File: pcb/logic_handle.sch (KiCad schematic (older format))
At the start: 13 parts, among them U1 NCP1117-3.3_TO252

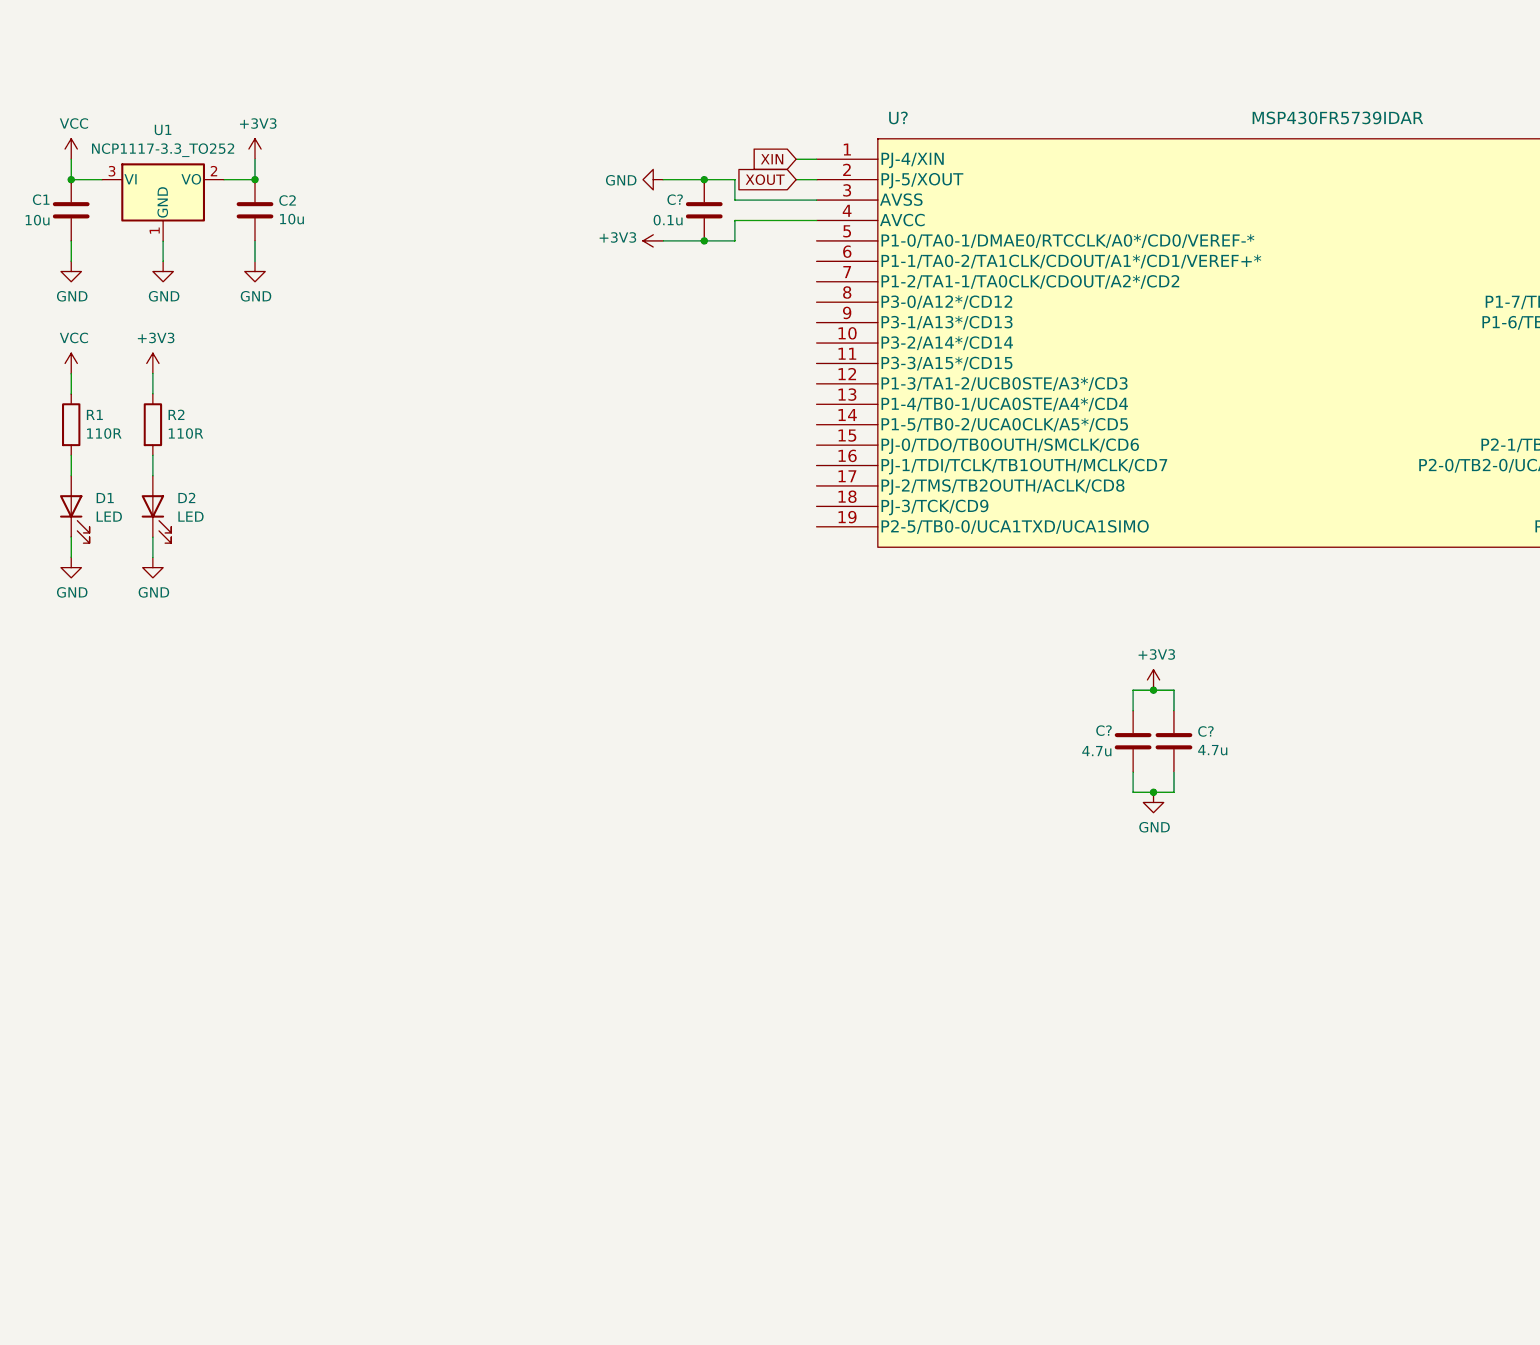
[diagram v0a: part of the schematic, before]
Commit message: [WIP] logic handle voltage translator
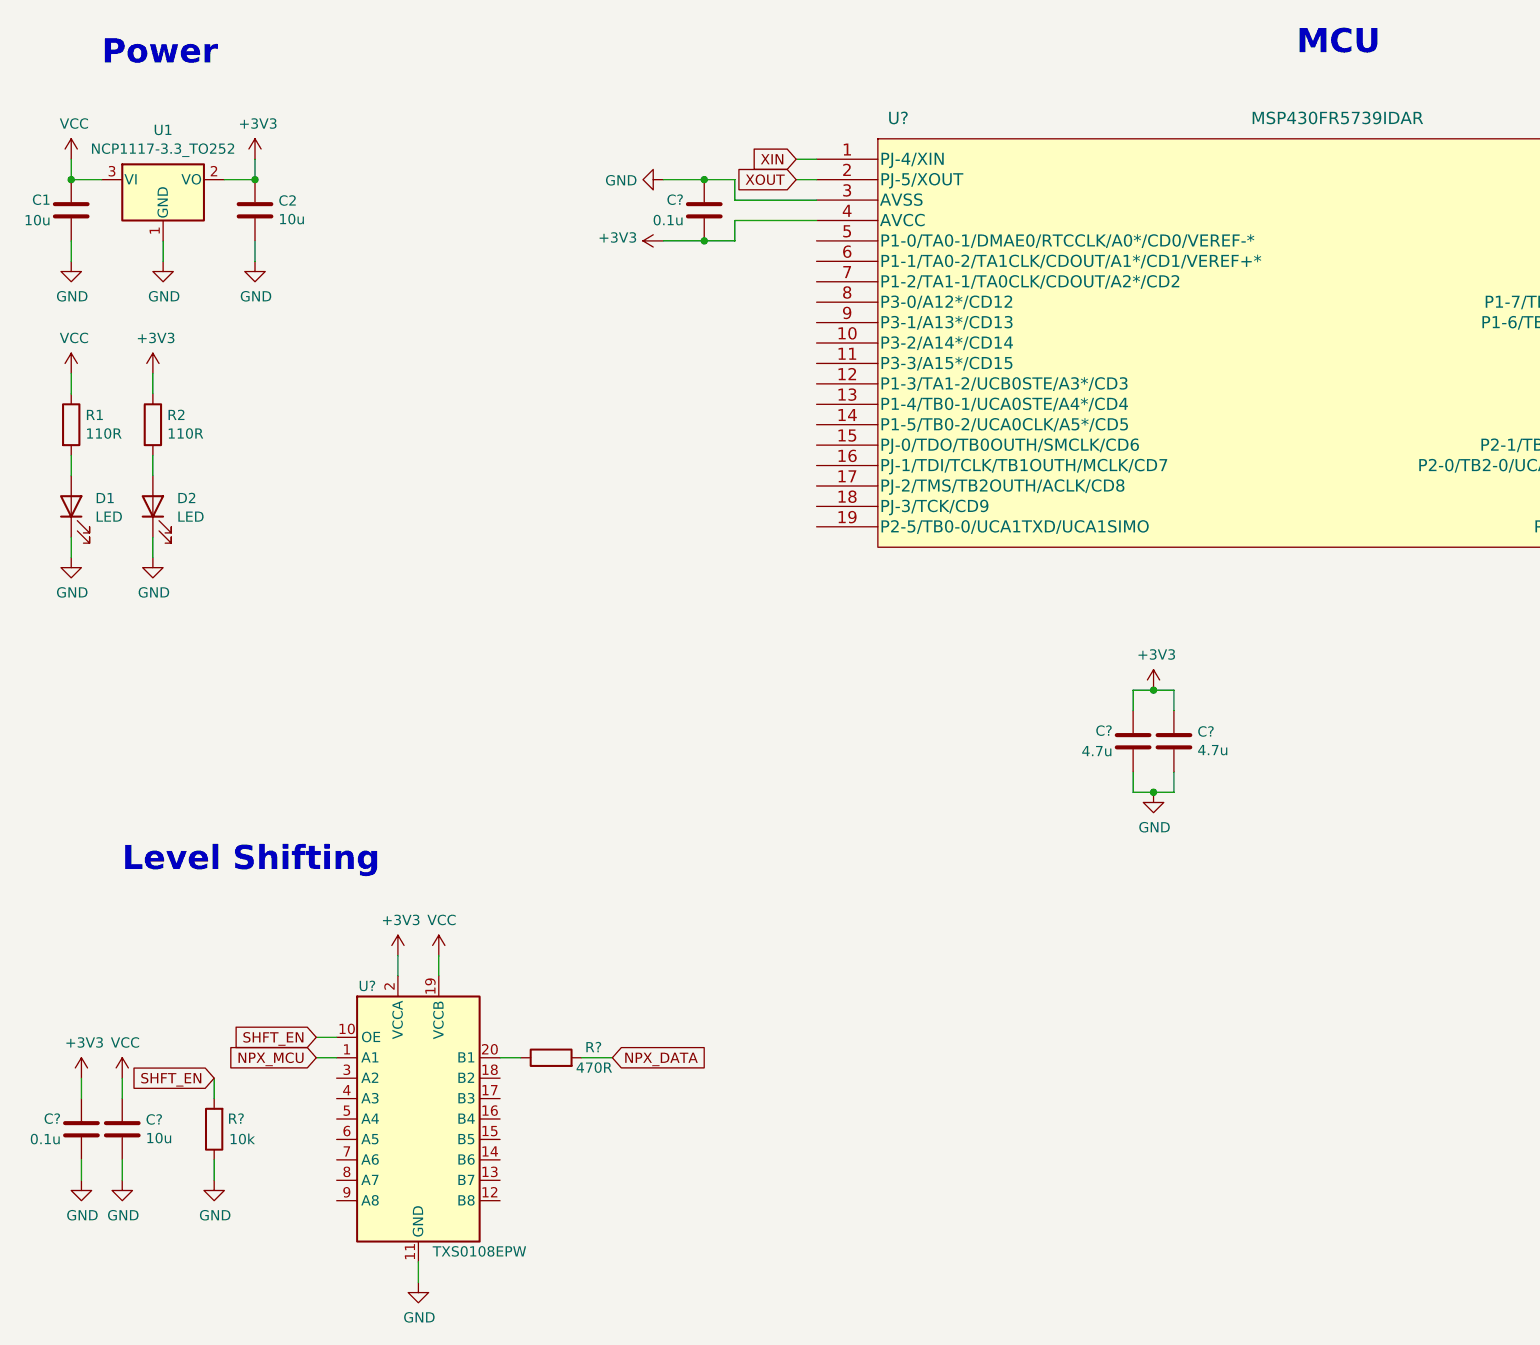
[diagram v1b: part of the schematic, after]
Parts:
- added C?: 0.1u, symbol Device:C
- added C?: 10u, symbol Device:C
- added R?: 10k, symbol Device:R
- added R?: 470R, symbol Device:R
- added U?: TXS0108EPW, Package_SO:TSSOP-20_4.4x6.5mm_P0.65mm, symbol Logic_LevelTranslator:TXS0108EPW
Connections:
- net +3V3: now also C?.2, U?.2 (VCCA)
- net GND: now also C?.1, C?.2, R?.1, U?.11 (GND)
- net VCC: now also C?.1, U?.19 (VCCB)
- new net: R?.1, U?.20 (B1)
- new net NPX_DATA: R?.2
- new net NPX_MCU: U?.1 (A1)
- new net SHFT_EN: R?.2, U?.10 (OE)
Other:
- note added: "Level Shifting"
- note added: "MCU"
- note added: "Power"
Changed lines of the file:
@@
 	6550 4450 6550 4350
 Connection ~ 6450 4450
+$Comp
+L Logic_LevelTranslator:TXS0108EPW U?
+U 1 1 619CE39A
+P 2850 6050
+F 0 "U?" H 2600 6700 50  0000 C CNN
+F 1 "TXS0108EPW" H 3150 5400 50  0000 C CNN
+F 2 "Package_SO:TSSOP-20_4.4x6.5mm_P0.65mm" H 2850 5300 50  0001 C CNN
+F 3 "www.ti.com/lit/ds/symlink/txs0108e.pdf" H 2850 5950 50  0001 C CNN
+F 4 "296-21527-1-ND" H 2850 6050 50  0001 C CNN "Digikey"
+	1    2850 6050
+	1    0    0    -1
+$EndComp
+$Comp
+L power:+3V3 #PWR?
+U 1 1 619CF59A
+P 2750 5250
+F 0 "#PWR?" H 2750 5100 50  0001 C CNN
+F 1 "+3V3" H 2765 5423 50  0000 C CNN
+F 2 "" H 2750 5250 50  0001 C CNN
+F 3 "" H 2750 5250 50  0001 C CNN
+	1    2750 5250
+	1    0    0    -1
+$EndComp
+Wire Wire Line
+	2750 5350 2750 5250
+$Comp
+L power:VCC #PWR?
+U 1 1 619D199B
+P 2950 5250
+F 0 "#PWR?" H 2950 5100 50  0001 C CNN
+F 1 "VCC" H 2965 5423 50  0000 C CNN
+F 2 "" H 2950 5250 50  0001 C CNN
+F 3 "" H 2950 5250 50  0001 C CNN
+	1    2950 5250
+	1    0    0    -1
+$EndComp
+Wire Wire Line
+	2950 5350 2950 5250
+$Comp
+L Device:R R?
+U 1 1 619D30A3
+P 1850 6100
+F 0 "R?" H 1700 6050 50  0000 L CNN
+F 1 "10k" H 1650 6150 50  0000 L CNN
+F 2 "" V 1780 6100 50  0001 C CNN
+F 3 "https://www.seielect.com/catalog/sei-rmcf_rmcp.pdf" H 1850 6100 50  0001 C CNN
+F 4 "RMCF0805JT110RCT-ND" H 1850 6100 50  0001 C CNN "Digikey"
+	1    1850 6100
+	-1   0    0    1
+$EndComp
+$Comp
+L power:GND #PWR?
+U 1 1 619D40ED
+P 1850 6350
+F 0 "#PWR?" H 1850 6100 50  0001 C CNN
+F 1 "GND" H 1855 6177 50  0000 C CNN
+F 2 "" H 1850 6350 50  0001 C CNN
+F 3 "" H 1850 6350 50  0001 C CNN
+	1    1850 6350
+	1    0    0    -1
+$EndComp
+Text GLabel 2350 5650 0    50   Input ~ 0
+SHFT_EN
+$Comp
+L power:GND #PWR?
+U 1 1 619D79C2
+P 2850 6850
+F 0 "#PWR?" H 2850 6600 50  0001 C CNN
+F 1 "GND" H 2855 6677 50  0000 C CNN
+F 2 "" H 2850 6850 50  0001 C CNN
+F 3 "" H 2850 6850 50  0001 C CNN
+	1    2850 6850
+	1    0    0    -1
+$EndComp
+Wire Wire Line
+	2850 6750 2850 6850
+$Comp
+L Device:C C?
+U 1 1 619D9BB2
+P 1200 6100
+F 0 "C?" H 1300 6050 50  0000 L CNN
+F 1 "0.1u" H 1300 6150 50  0000 L CNN
+F 2 "" H 1238 5950 50  0001 C CNN
+F 3 "~" H 1200 6100 50  0001 C CNN
+	1    1200 6100
+	-1   0    0    1
+$EndComp
+$Comp
+L power:GND #PWR?
+U 1 1 619DC720
+P 1200 6350
+F 0 "#PWR?" H 1200 6100 50  0001 C CNN
+F 1 "GND" H 1205 6177 50  0000 C CNN
+F 2 "" H 1200 6350 50  0001 C CNN
+F 3 "" H 1200 6350 50  0001 C CNN
+	1    1200 6350
+	1    0    0    -1
+$EndComp
+$Comp
+L power:GND #PWR?
+U 1 1 619DD6CD
+P 1400 6350
+F 0 "#PWR?" H 1400 6100 50  0001 C CNN
+F 1 "GND" H 1405 6177 50  0000 C CNN
+F 2 "" H 1400 6350 50  0001 C CNN
+F 3 "" H 1400 6350 50  0001 C CNN
+	1    1400 6350
+	1    0    0    -1
+$EndComp
+Wire Wire Line
+	1200 6350 1200 6250
+Wire Wire Line
+	1400 6350 1400 6250
+$Comp
+L Device:C C?
+U 1 1 619DFAAB
+P 1400 6100
+F 0 "C?" H 1515 6146 50  0000 L CNN
+F 1 "10u" H 1515 6055 50  0000 L CNN
+F 2 "" H 1438 5950 50  0001 C CNN
+F 3 "~" H 1400 6100 50  0001 C CNN
+	1    1400 6100
+	1    0    0    -1
+$EndComp
+$Comp
+L power:+3V3 #PWR?
+U 1 1 619E1DEA
+P 1200 5850
+F 0 "#PWR?" H 1200 5700 50  0001 C CNN
+F 1 "+3V3" H 1215 6023 50  0000 C CNN
+F 2 "" H 1200 5850 50  0001 C CNN
+F 3 "" H 1200 5850 50  0001 C CNN
+	1    1200 5850
+	1    0    0    -1
+$EndComp
+$Comp
+L power:VCC #PWR?
+U 1 1 619E251A
+P 1400 5850
+F 0 "#PWR?" H 1400 5700 50  0001 C CNN
+F 1 "VCC" H 1415 6023 50  0000 C CNN
+F 2 "" H 1400 5850 50  0001 C CNN
+F 3 "" H 1400 5850 50  0001 C CNN
+	1    1400 5850
+	1    0    0    -1
+$EndComp
+Wire Wire Line
+	1200 5850 1200 5950
+Wire Wire Line
+	1400 5850 1400 5950
+Text Notes 1400 4850 0    118  ~ 24
+Level Shifting
+Text Notes 7150 850  0    118  ~ 24
+MCU
+Text Notes 1300 900  0    118  ~ 24
+Power
+$Comp
+L Device:R R?
+U 1 1 619F32E8
+P 3500 5750
+F 0 "R?" V 3550 5500 50  0000 L CNN
+F 1 "470R" V 3450 5450 50  0000 L CNN
+F 2 "" V 3430 5750 50  0001 C CNN
+F 3 "https://www.seielect.com/catalog/sei-rmcf_rmcp.pdf" H 3500 5750 50  0001 C CNN
+F 4 "RMCF0805JT110RCT-ND" H 3500 5750 50  0001 C CNN "Digikey"
+	1    3500 5750
+	0    -1   -1   0
+$EndComp
+Wire Wire Line
+	3350 5750 3250 5750
+Wire Wire Line
+	3650 5750 3800 5750
+Text GLabel 3800 5750 2    50   Input ~ 0
+NPX_DATA
+Text GLabel 2350 5750 0    50   Input ~ 0
+NPX_MCU
+Wire Wire Line
+	1850 6250 1850 6350
+Text GLabel 1850 5850 0    50   Input ~ 0
+SHFT_EN
+Wire Wire Line
+	1850 5850 1850 5950
+Wire Wire Line
+	2350 5650 2450 5650
+Wire Wire Line
+	2350 5750 2450 5750
 $EndSCHEMATC

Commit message: [WIP]: Logic handle schematic and layout complete
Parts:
- added C8, C9: 15p, Capacitor_SMD:C_0805_2012Metric, symbol Device:C
- added J1: Conn_01x05_Male, Connector_PinHeader_2.54mm:PinHeader_1x05_P2.54mm_Vertical, symbol Connector:Conn_01x05_Male
- added JP1, JP10, JP2, JP3, JP4, JP5, JP6, JP7, JP8, JP9: Jumper_3_Bridged12, Jumper:SolderJumper-3_P1.3mm_Bridged2Bar12_Pad1.0x1.5mm, symbol Jumper:Jumper_3_Bridged12
- added JP11: Jumper, Jumper:SolderJumper-2_P1.3mm_Bridged2Bar_Pad1.0x1.5mm, symbol Device:Jumper
- added Q1: BSS214NW, Package_TO_SOT_SMD:SOT-323_SC-70, symbol Transistor_FET:BSS214NW
- added R5: 47k, Resistor_SMD:R_0805_2012Metric, symbol Device:R
- added R6, R8: 10k, Resistor_SMD:R_0805_2012Metric, symbol Device:R
- added R7: 110R, Resistor_SMD:R_0805_2012Metric, symbol Device:R
- added R9: 1M, Resistor_SMD:R_0805_2012Metric, symbol Device:R
- added SW1: SW_Push, Button_Switch_SMD:SW_SPST_TL3342, symbol Switch:SW_Push
- added TP1, TP10, TP11, TP12, TP2, TP3, TP4, TP5, TP6, TP7, TP8, TP9: TestPoint, TestPoint:TestPoint_Pad_2.0x2.0mm, symbol Connector:TestPoint
- added Y1: Crystal, Gigahawk:Crystal_SMD_AWSZT-CV-2Pin_3.7x3.1mm, symbol Device:Crystal
- C1, C2: footprint (none) -> Capacitor_SMD:C_0805_2012Metric
- C10, C11, C3, C4, C5, C6, C7: renamed from C?; footprint (none) -> Capacitor_SMD:C_0805_2012Metric
- R1, R2: footprint (none) -> Resistor_SMD:R_0805_2012Metric
- R3, R4: renamed from R?; footprint (none) -> Resistor_SMD:R_0805_2012Metric
- gave numbers to parts that had none: 2
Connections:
- net +3V3: now also R5.2, TP2.1
- net GND: now also C8.2, C9.1, J1.4 (Pin_4), JP11.1, Q1.3 (D), R8.1, SW1.2, TP3.1
- net NPX_MCU: now also JP1.2 (C), JP6.2 (C); no longer U2.1 (A1)
- net SBWTCK: now also J1.2 (Pin_2)
- net SBWTDIO: now also J1.3 (Pin_3), R5.1, SW1.1
- net SHFT_EN: now also U3.29 (P3-7/TB2-2), TP11.1
- net VCC: now also R6.2, R7.2, TP1.1
- net XIN: now also C8.1, R9.1, Y1.1
- net XOUT: now also C9.2, R9.2, Y1.2
- net BTN1_AUX: now reaches U3.10 (P3-2/A14*/CD14)
- net BTN1_AUX: now also JP4.3 (B)
- net BTN2_AUX: now reaches U3.11 (P3-3/A15*/CD15)
- net BTN2_AUX: now also JP5.3 (B)
- net NPX_DBG_CLK_AUX: now reaches U3.14 (P1-5/TB0-2/UCA0CLK/A5*/CD5)
- net NPX_DBG_CLK_AUX: now also TP5.1
- net LED1_MAIN: now reaches U3.15 (PJ-0/TDO/TB0OUTH/SMCLK/CD6)
- net LED1_MAIN: now also JP2.1 (A)
- net LED2_MAIN: now reaches U3.16 (PJ-1/TDI/TCLK/TB1OUTH/MCLK/CD7)
- net LED2_MAIN: now also JP3.1 (A)
- net LED1_AUX: now reaches U3.17 (PJ-2/TMS/TB2OUTH/ACLK/CD8)
- net LED1_AUX: now also JP2.3 (B)
- net LED2_AUX: now reaches U3.18 (PJ-3/TCK/CD9)
- net LED2_AUX: now also JP3.3 (B)
- net UART_TXD: now reaches U3.19 (P2-5/TB0-0/UCA1TXD/UCA1SIMO)
- net UART_TXD: now also J1.1 (Pin_1)
- net UART_RXD: now reaches U3.20 (P2-6/TB1-0/UCA1RXD/UCA1SOMI)
- net UART_RXD: now also J1.5 (Pin_5)
- net NPX_AUX: now reaches U3.23 (P2-0/TB2-0/UCA0TXD/UCA0SIMO/TB0CLK/ACLK)
- net NPX_AUX: now also JP1.3 (B)
- net NPX_DBG_CLK_MAIN: now reaches U3.25 (P2-2/TB2-2/UCB0CLK/TB1-0)
- net NPX_DBG_CLK_MAIN: now also TP4.1
- net NPX_MAIN: now reaches U3.30 (P1-6/TB1-1/UCB0SIMO/UCB0SDA/TA0-0)
- net NPX_MAIN: now also JP1.1 (A)
- net BTN1_MAIN: now reaches U3.8 (P3-0/A12*/CD12)
- net BTN1_MAIN: now also JP4.1 (A)
- net BTN2_MAIN: now reaches U3.9 (P3-1/A13*/CD13)
- net BTN2_MAIN: now also JP5.1 (A)
- net BTN2: now reaches U2.15 (B5)
- net BTN2: now also JP10.3 (B), TP10.1
- net BTN+: now reaches U2.16 (B4)
- net BTN+: now also JP9.3 (B), R6.1, TP9.1
- net IC_BTN_LED: now reaches U2.17 (B3)
- net IC_BTN_LED: now also JP8.3 (B), TP8.1
- net LED1: now reaches U2.18 (B2)
- net LED1: now also JP7.3 (B), Q1.1 (G), R8.2, TP7.1
- net NPX_MCU_BYPASS: now reaches R4.1, U2.20 (B1)
- net NPX_MCU_BYPASS: now also JP6.3 (B), TP12.1
- net LED1_MCU_SHIFT: now reaches U2.3 (A2)
- net LED1_MCU_SHIFT: now also JP7.1 (A)
- net LED2_MCU_SHIFT: now reaches U2.4 (A3)
- net LED2_MCU_SHIFT: now also JP8.1 (A)
- net BTN1_MCU_SHIFT: now reaches U2.5 (A4)
- net BTN1_MCU_SHIFT: now also JP9.1 (A)
- net BTN2_MCU_SHIFT: now reaches U2.6 (A5)
- net BTN2_MCU_SHIFT: now also JP10.1 (A)
- net NPX_DATA renamed NPX
- net NPX: now also TP6.1
- new net BTN-: JP11.2
- new net BTN1_MCU: JP4.2 (C), JP9.2 (C)
- new net BTN2_MCU: JP10.2 (C), JP5.2 (C)
- new net LED+: R7.1
- new net LED-: Q1.2 (S)
- new net LED1_MCU: JP2.2 (C), JP7.2 (C)
- new net LED2_MCU: JP3.2 (C), JP8.2 (C)
- new net NPX_MCU_SHIFT: JP6.1 (A), U2.1 (A1)
- no-connect marks 0 -> 19
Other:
- note added: "24MHz or DNI"
- note added: "Jumper here to avoid\nGND net being renamed"
- note added: "Level Shifter Bypass"
- note added: "Programming"
- note added: "Reset\nSwitch"
- moved on the sheet: C3, C4, C6, C7, R3, R4, U2

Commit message: [WIP]: Finish logic PCB
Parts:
- C1, C2, C4: Digikey (none) -> 1276-6456-1-ND
- C10: Digikey (none) -> 478-10438-1-ND
- C11, C3, C5: Digikey (none) -> 478-10836-1-ND
- C6, C7: Digikey (none) -> 1276-1259-1-ND
- C8, C9: Digikey (none) -> 478-1306-1-ND
- U3: Digikey (none) -> 296-29235-1-ND
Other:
- note added: "Common"
- note added: "Testpoints"
- moved on the sheet: TP1, TP10, TP11, TP12, TP2, TP3, TP4, TP5, TP6, TP7, TP8, TP9

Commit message: pcb: Cleanup BOM items (#7)
Replaced out of stock components with substitutes
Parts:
- R3, R6, R8: Digikey RMCF0805JT110RCT-ND -> RMCF0805JT10K0CT-ND
- R4: Digikey RMCF0805JT110RCT-ND -> A129745CT-ND
- R5: Digikey RMCF0805JT110RCT-ND -> A130144CT-ND
- R9: Digikey RMCF0805JT110RCT-ND -> A106058CT-ND
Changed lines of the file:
@@
 F 2 "Resistor_SMD:R_0805_2012Metric" V 1380 4500 50  0001 C CNN
 F 3 "https://www.seielect.com/catalog/sei-rmcf_rmcp.pdf" H 1450 4500 50  0001 C CNN
-F 4 "RMCF0805JT110RCT-ND" H 1450 4500 50  0001 C CNN "Digikey"
+F 4 "RMCF0805JT10K0CT-ND" H 1450 4500 50  0001 C CNN "Digikey"
 	1    1450 4500
 	-1   0    0    1
@@
 F 1 "470R" V 3450 4500 50  0000 L CNN
 F 2 "Resistor_SMD:R_0805_2012Metric" V 3430 4800 50  0001 C CNN
-F 3 "https://www.seielect.com/catalog/sei-rmcf_rmcp.pdf" H 3500 4800 50  0001 C CNN
-F 4 "RMCF0805JT110RCT-ND" H 3500 4800 50  0001 C CNN "Digikey"
+F 3 "https://www.te.com/commerce/DocumentDelivery/DDEController?Action=srchrtrv&DocNm=1773204-3&DocType=DS&DocLang=English" H 3500 4800 50  0001 C CNN
+F 4 "A129745CT-ND" H 3500 4800 50  0001 C CNN "Digikey"
 	1    3500 4800
 	0    -1   -1   0
@@
 F 1 "1M" V 9650 4100 50  0000 L CNN
 F 2 "Resistor_SMD:R_0805_2012Metric" V 9530 4000 50  0001 C CNN
-F 3 "https://www.seielect.com/catalog/sei-rmcf_rmcp.pdf" H 9600 4000 50  0001 C CNN
-F 4 "RMCF0805JT110RCT-ND" H 9600 4000 50  0001 C CNN "Digikey"
+F 3 "https://www.te.com/commerce/DocumentDelivery/DDEController?Action=srchrtrv&DocNm=1773204&DocType=DS&DocLang=English" H 9600 4000 50  0001 C CNN
+F 4 "A106058CT-ND" H 9600 4000 50  0001 C CNN "Digikey"
 	1    9600 4000
 	0    -1   -1   0
@@
 F 2 "Resistor_SMD:R_0805_2012Metric" V 8030 7850 50  0001 C CNN
 F 3 "https://www.seielect.com/catalog/sei-rmcf_rmcp.pdf" H 8100 7850 50  0001 C CNN
-F 4 "RMCF0805JT110RCT-ND" H 8100 7850 50  0001 C CNN "Digikey"
+F 4 "RMCF0805JT10K0CT-ND" H 8100 7850 50  0001 C CNN "Digikey"
 	1    8100 7850
 	-1   0    0    1
@@
 F 2 "Resistor_SMD:R_0805_2012Metric" V 9380 8750 50  0001 C CNN
 F 3 "https://www.seielect.com/catalog/sei-rmcf_rmcp.pdf" H 9450 8750 50  0001 C CNN
-F 4 "RMCF0805JT110RCT-ND" H 9450 8750 50  0001 C CNN "Digikey"
+F 4 "RMCF0805JT10K0CT-ND" H 9450 8750 50  0001 C CNN "Digikey"
 	1    9450 8750
 	-1   0    0    1
@@
 F 1 "47k" H 6750 4050 50  0000 L CNN
 F 2 "Resistor_SMD:R_0805_2012Metric" V 6880 4000 50  0001 C CNN
-F 3 "https://www.seielect.com/catalog/sei-rmcf_rmcp.pdf" H 6950 4000 50  0001 C CNN
-F 4 "RMCF0805JT110RCT-ND" H 6950 4000 50  0001 C CNN "Digikey"
+F 3 "https://www.te.com/commerce/DocumentDelivery/DDEController?Action=srchrtrv&DocNm=1773204-3&DocType=DS&DocLang=English" H 6950 4000 50  0001 C CNN
+F 4 "A130144CT-ND" H 6950 4000 50  0001 C CNN "Digikey"
 	1    6950 4000
 	-1   0    0    1
